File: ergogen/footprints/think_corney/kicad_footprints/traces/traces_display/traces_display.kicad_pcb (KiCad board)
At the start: 2 copper layers, 130.3 x 86.5 mm, 112 parts

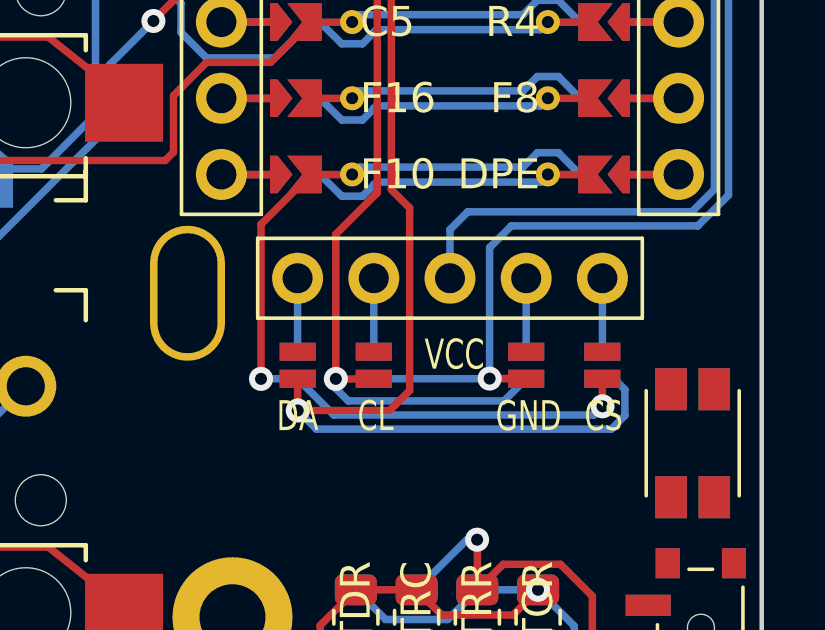
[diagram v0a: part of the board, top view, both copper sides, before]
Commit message: Traces: Added remaining missing traces
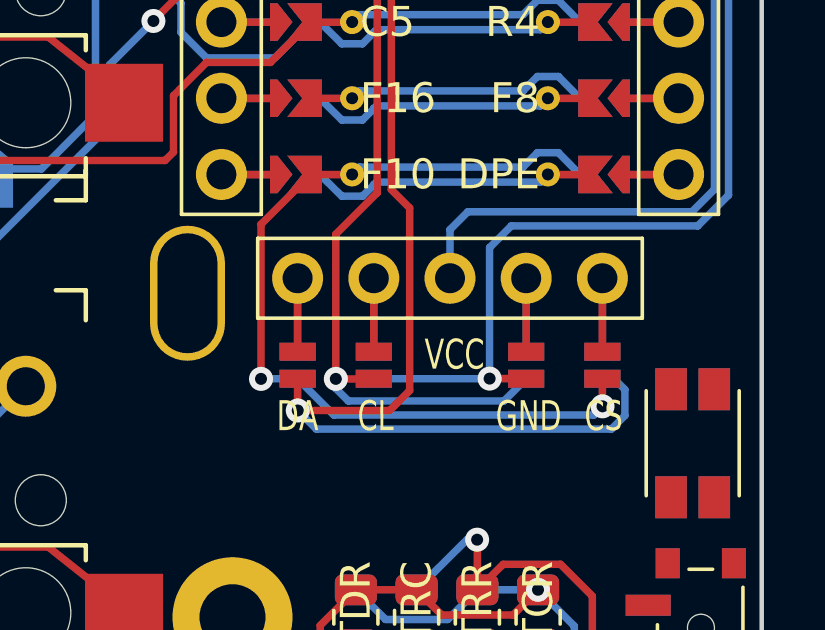
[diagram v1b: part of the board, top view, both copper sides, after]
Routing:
- net DISP1_5: track 2.45 -> 4.90 mm
- net DISP1_4: track 2.45 -> 4.90 mm
- net DISP1_2: track 2.45 -> 4.90 mm
- net DISP1_1: track 2.45 -> 4.90 mm
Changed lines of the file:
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@@
   (segment locked (start -26.385959 9.854694) (end -25.185959 8.624694) (width 0.25) (layer "B.Cu") (net 67))
   (segment locked (start -16.195959 8.654694) (end -16.405959 8.654694) (width 0.25) (layer "B.Cu") (net 67))
+  (segment (start -5.08 19.15) (end -5.08 16.7) (width 0.25) (layer "F.Cu") (net 68))
   (segment (start -5.08 16.7) (end -5.08 19.15) (width 0.25) (layer "B.Cu") (net 68))
+  (segment (start -2.54 19.15) (end -2.54 16.7) (width 0.25) (layer "F.Cu") (net 69))
   (segment (start -2.54 16.7) (end -2.54 19.15) (width 0.25) (layer "B.Cu") (net 69))
+  (segment (start 2.54 19.15) (end 2.54 16.7) (width 0.25) (layer "F.Cu") (net 70))
   (segment (start 2.54 16.7) (end 2.54 19.15) (width 0.25) (layer "B.Cu") (net 70))
+  (segment (start 5.08 19.15) (end 5.08 16.7) (width 0.25) (layer "F.Cu") (net 71))
   (segment (start 5.08 16.7) (end 5.08 19.15) (width 0.25) (layer "B.Cu") (net 71))
   (segment locked (start -7.985959 35.534694) (end -6.995959 34.554694) (width 0.25) (layer "F.Cu") (net 72))
